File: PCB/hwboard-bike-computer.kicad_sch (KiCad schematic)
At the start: 0 parts

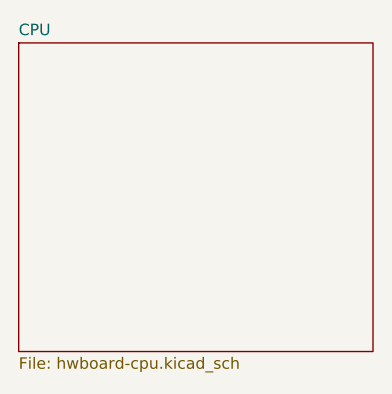
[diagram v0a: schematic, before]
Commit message: Remove temporary and configuration files related to the bike computer project, including lock, PCB, PRL, and project files.
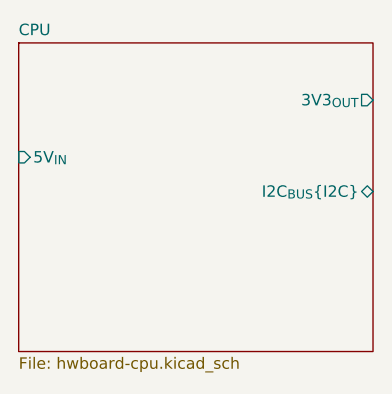
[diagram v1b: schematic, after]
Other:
- sheet CPU ports: added 3V3_{OUT}, 5V_{IN}, I2C_{BUS}{I2C}; removed none
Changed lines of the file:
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@@
+			)
+		)
+		(pin "3V3_{OUT}" output
+			(at 170.18 88.9 0)
+			(effects
+				(font
+					(size 1.27 1.27)
+				)
+				(justify right)
+			)
+		)
+		(pin "I2C_{BUS}{I2C}" bidirectional
+			(at 170.18 99.06 0)
+			(effects
+				(font
+					(size 1.27 1.27)
+				)
+				(justify right)
+			)
+		)
+		(pin "5V_{IN}" input
+			(at 130.81 95.25 180)
+			(effects
+				(font
+					(size 1.27 1.27)
+				)
+				(justify left)
 			)
 		)

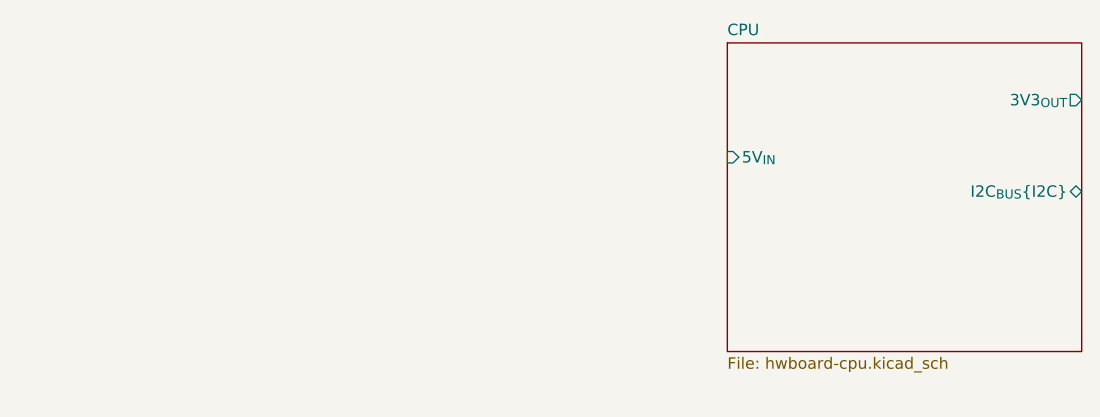
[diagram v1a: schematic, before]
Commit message: add gnss schematics and footprint
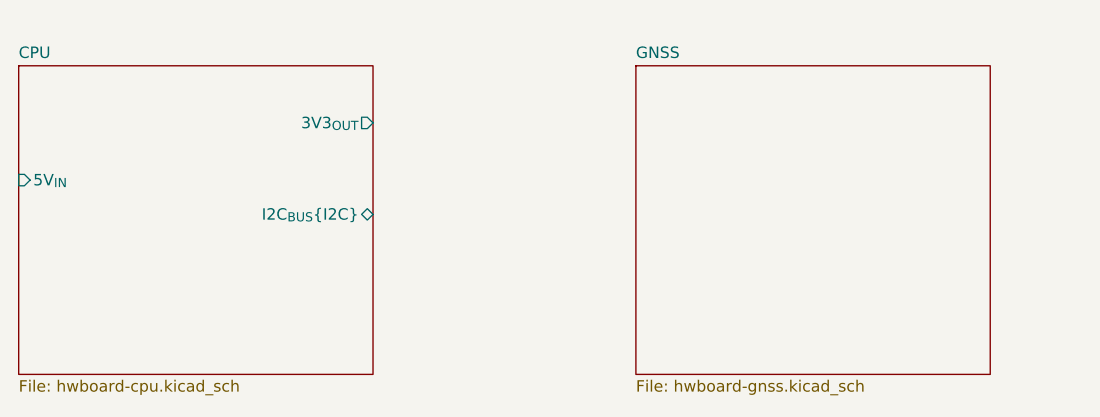
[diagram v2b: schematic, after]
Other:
- added sheet GNSS (hwboard-gnss.kicad_sch)
- title: (none) -> HWBoard Bike Computer
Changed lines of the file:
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@@
 	(generator_version "9.0")
 	(paper "A4")
+	(title_block
+		(title "HWBoard Bike Computer")
+		(date "2025-10-22")
+		(rev "0.1")
+	)
 	(sheet
-		(at 130.81 82.55)
+		(at 52.07 85.09)
 		(size 39.37 34.29)
 		(exclude_from_sim no)
@@
 		)
 		(property "Sheetname" "CPU"
-			(at 130.81 81.8384 0)
+			(at 52.07 84.3784 0)
 			(effects
 				(font
@@
 		)
 		(property "Sheetfile" "hwboard-cpu.kicad_sch"
-			(at 130.81 117.4246 0)
+			(at 52.07 119.9646 0)
 			(effects
 				(font
@@
 		)
 		(pin "3V3_{OUT}" output
-			(at 170.18 88.9 0)
+			(at 91.44 91.44 0)
 			(effects
 				(font
@@
 		)
 		(pin "I2C_{BUS}{I2C}" bidirectional
-			(at 170.18 99.06 0)
+			(at 91.44 101.6 0)
 			(effects
 				(font
@@
 		)
 		(pin "5V_{IN}" input
-			(at 130.81 95.25 180)
+			(at 52.07 97.79 180)
 			(effects
 				(font
@@
 				)
 			)
+		)
+	)
+	(sheet
+		(at 120.65 85.09)
+		(size 39.37 34.29)
+		(exclude_from_sim no)
+		(in_bom yes)
+		(on_board yes)
+		(dnp no)
+		(fields_autoplaced yes)
+		(stroke
+			(width 0.1524)
+			(type solid)
+		)
+		(fill
+			(color 0 0 0 0.0000)
+		)
+		(property "Sheetname" "GNSS"
+			(at 120.65 84.3784 0)
+			(effects
+				(font
+					(size 1.27 1.27)
+				)
+				(justify left bottom)
+			)
+		)
+		(property "Sheetfile" "hwboard-gnss.kicad_sch"
+			(at 120.65 119.9646 0)
+			(effects
+				(font
+					(size 1.27 1.27)
+				)
+				(justify left top)
+			)
+		)
+		(instances
+			(project "hwboard-bike-computer"
+				(path "/8c0f76b9-ee42-4bcf-bb95-09772e367402"
+					(page "3")
+				)
+			)

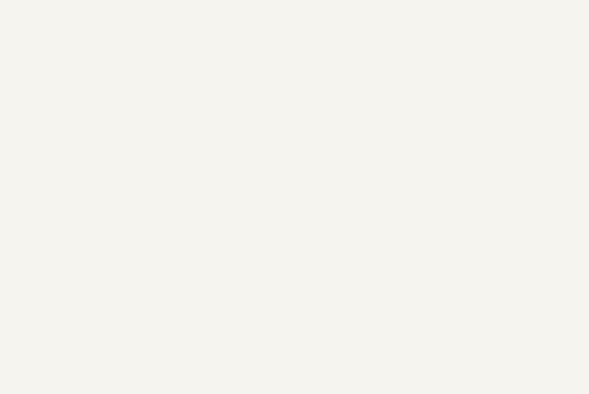
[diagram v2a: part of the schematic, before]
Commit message: add screen sheet
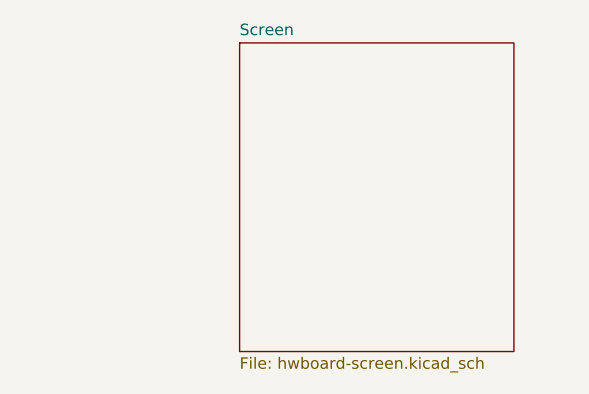
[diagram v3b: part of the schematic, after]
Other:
- added sheet Screen (hwboard-screen.kicad_sch)
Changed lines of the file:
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@@
+	)
+	(sheet
+		(at 201.93 85.09)
+		(size 30.48 34.29)
+		(exclude_from_sim no)
+		(in_bom yes)
+		(on_board yes)
+		(dnp no)
+		(fields_autoplaced yes)
+		(stroke
+			(width 0.1524)
+			(type solid)
+		)
+		(fill
+			(color 0 0 0 0.0000)
+		)
+		(property "Sheetname" "Screen"
+			(at 201.93 84.3784 0)
+			(effects
+				(font
+					(size 1.27 1.27)
+				)
+				(justify left bottom)
+			)
+		)
+		(property "Sheetfile" "hwboard-screen.kicad_sch"
+			(at 201.93 119.9646 0)
+			(effects
+				(font
+					(size 1.27 1.27)
+				)
+				(justify left top)
+			)
+		)
+		(instances
+			(project "hwboard-bike-computer"
+				(path "/8c0f76b9-ee42-4bcf-bb95-09772e367402"
+					(page "4")
+				)
+			)
+		)
 	)
 	(sheet

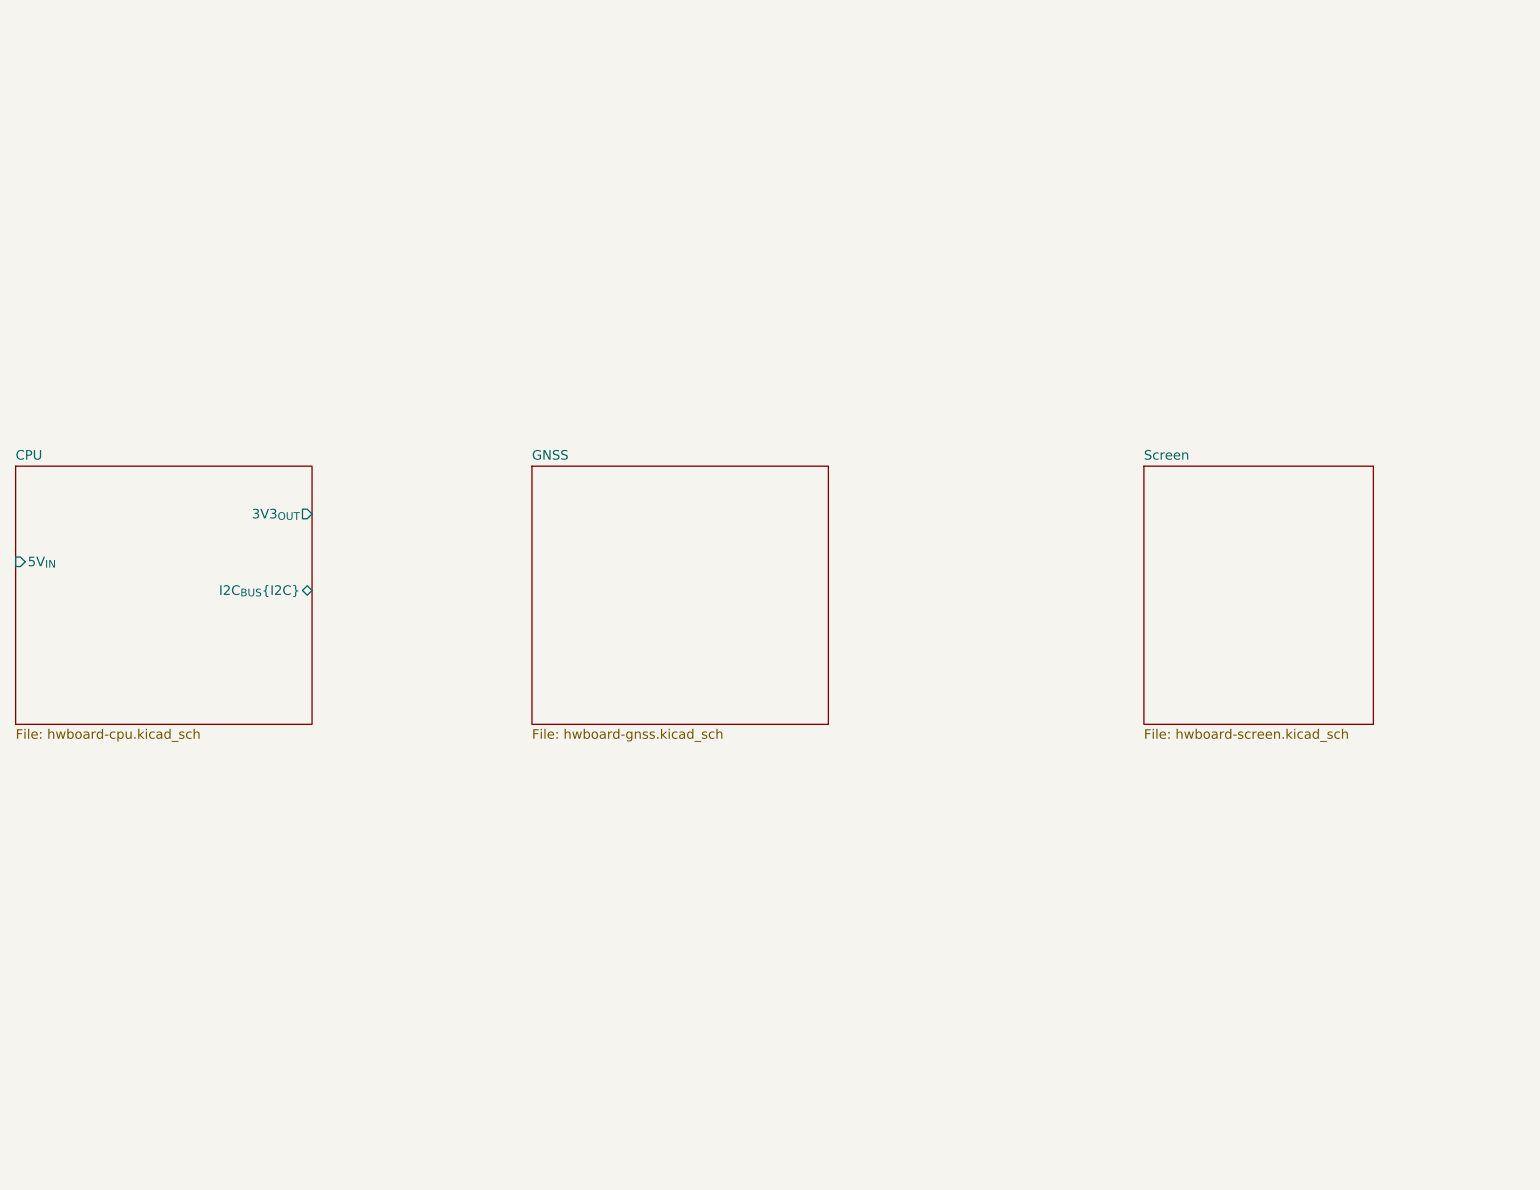
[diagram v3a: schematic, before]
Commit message: add others hierarchicals sheets
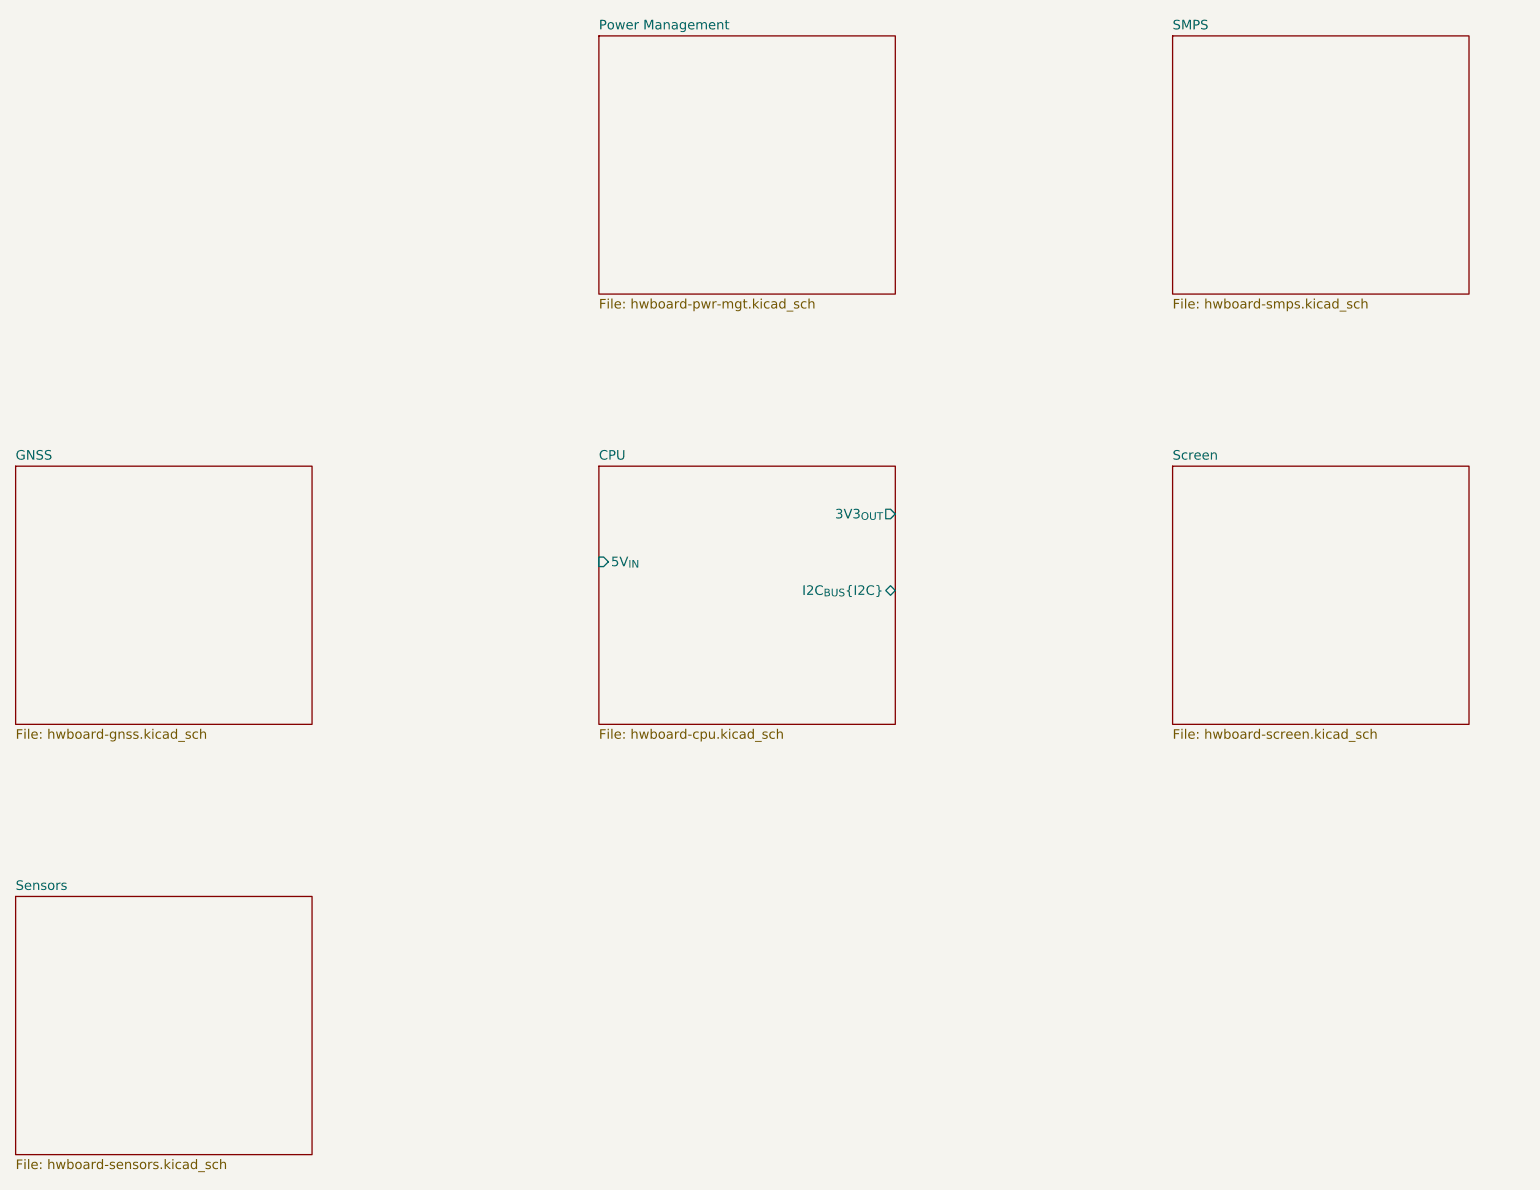
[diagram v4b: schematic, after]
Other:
- added sheet Power Management (hwboard-pwr-mgt.kicad_sch)
- added sheet SMPS (hwboard-smps.kicad_sch)
- added sheet Sensors (hwboard-sensors.kicad_sch)
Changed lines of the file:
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@@
+	)
+	(sheet
+		(at 52.07 142.24)
+		(size 39.37 34.29)
+		(exclude_from_sim no)
+		(in_bom yes)
+		(on_board yes)
+		(dnp no)
+		(fields_autoplaced yes)
+		(stroke
+			(width 0.1524)
+			(type solid)
+		)
+		(fill
+			(color 0 0 0 0.0000)
+		)
+		(property "Sheetname" "Sensors"
+			(at 52.07 141.5284 0)
+			(effects
+				(font
+					(size 1.27 1.27)
+				)
+				(justify left bottom)
+			)
+		)
+		(property "Sheetfile" "hwboard-sensors.kicad_sch"
+			(at 52.07 177.1146 0)
+			(effects
+				(font
+					(size 1.27 1.27)
+				)
+				(justify left top)
+			)
+		)
+		(instances
+			(project "hwboard-bike-computer"
+				(path "/8c0f76b9-ee42-4bcf-bb95-09772e367402"
+					(page "7")
+				)
+			)
+		)
+	)
+	(sheet
+		(at 129.54 85.09)
+		(size 39.37 34.29)
+		(exclude_from_sim no)
+		(in_bom yes)
+		(on_board yes)
+		(dnp no)
+		(fields_autoplaced yes)
+		(stroke
+			(width 0.1524)
+			(type solid)
+		)
+		(fill
+			(color 0 0 0 0.0000)
+		)
+		(property "Sheetname" "CPU"
+			(at 129.54 84.3784 0)
+			(effects
+				(font
+					(size 1.27 1.27)
+				)
+				(justify left bottom)
+			)
+		)
+		(property "Sheetfile" "hwboard-cpu.kicad_sch"
+			(at 129.54 119.9646 0)
+			(effects
+				(font
+					(size 1.27 1.27)
+				)
+				(justify left top)
+			)
+		)
+		(pin "3V3_{OUT}" output
+			(at 168.91 91.44 0)
+			(effects
+				(font
+					(size 1.27 1.27)
+				)
+				(justify right)
+			)
+		)
+		(pin "I2C_{BUS}{I2C}" bidirectional
+			(at 168.91 101.6 0)
+			(effects
+				(font
+					(size 1.27 1.27)
+				)
+				(justify right)
+			)
+		)
+		(pin "5V_{IN}" input
+			(at 129.54 97.79 180)
+			(effects
+				(font
+					(size 1.27 1.27)
+				)
+				(justify left)
+			)
+		)
+		(instances
+			(project "hwboard-bike-computer"
+				(path "/8c0f76b9-ee42-4bcf-bb95-09772e367402"
+					(page "2")
+				)
+			)
+		)
+	)
+	(sheet
+		(at 205.74 85.09)
+		(size 39.37 34.29)
+		(exclude_from_sim no)
+		(in_bom yes)
+		(on_board yes)
+		(dnp no)
+		(fields_autoplaced yes)
+		(stroke
+			(width 0.1524)
+			(type solid)
+		)
+		(fill
+			(color 0 0 0 0.0000)
+		)
+		(property "Sheetname" "Screen"
+			(at 205.74 84.3784 0)
+			(effects
+				(font
+					(size 1.27 1.27)
+				)
+				(justify left bottom)
+			)
+		)
+		(property "Sheetfile" "hwboard-screen.kicad_sch"
+			(at 205.74 119.9646 0)
+			(effects
+				(font
+					(size 1.27 1.27)
+				)
+				(justify left top)
+			)
+		)
+		(instances
+			(project "hwboard-bike-computer"
+				(path "/8c0f76b9-ee42-4bcf-bb95-09772e367402"
+					(page "4")
+				)
+			)
+		)
+	)
+	(sheet
+		(at 129.54 27.94)
+		(size 39.37 34.29)
+		(exclude_from_sim no)
+		(in_bom yes)
+		(on_board yes)
+		(dnp no)
+		(fields_autoplaced yes)
+		(stroke
+			(width 0.1524)
+			(type solid)
+		)
+		(fill
+			(color 0 0 0 0.0000)
+		)
+		(property "Sheetname" "Power Management"
+			(at 129.54 27.2284 0)
+			(effects
+				(font
+					(size 1.27 1.27)
+				)
+				(justify left bottom)
+			)
+		)
+		(property "Sheetfile" "hwboard-pwr-mgt.kicad_sch"
+			(at 129.54 62.8146 0)
+			(effects
+				(font
+					(size 1.27 1.27)
+				)
+				(justify left top)
+			)
+		)
+		(instances
+			(project "hwboard-bike-computer"
+				(path "/8c0f76b9-ee42-4bcf-bb95-09772e367402"
+					(page "5")
+				)
+			)
+		)
+	)
+	(sheet
+		(at 205.74 27.94)
+		(size 39.37 34.29)
+		(exclude_from_sim no)
+		(in_bom yes)
+		(on_board yes)
+		(dnp no)
+		(fields_autoplaced yes)
+		(stroke
+			(width 0.1524)
+			(type solid)
+		)
+		(fill
+			(color 0 0 0 0.0000)
+		)
+		(property "Sheetname" "SMPS"
+			(at 205.74 27.2284 0)
+			(effects
+				(font
+					(size 1.27 1.27)
+				)
+				(justify left bottom)
+			)
+		)
+		(property "Sheetfile" "hwboard-smps.kicad_sch"
+			(at 205.74 62.8146 0)
+			(effects
+				(font
+					(size 1.27 1.27)
+				)
+				(justify left top)
+			)
+		)
+		(instances
+			(project "hwboard-bike-computer"
+				(path "/8c0f76b9-ee42-4bcf-bb95-09772e367402"
+					(page "6")
+				)
+			)
+		)
 	)
 	(sheet
@@
 			(color 0 0 0 0.0000)
 		)
-		(property "Sheetname" "CPU"
+		(property "Sheetname" "GNSS"
 			(at 52.07 84.3784 0)
 			(effects
@@
 			)
 		)
-		(property "Sheetfile" "hwboard-cpu.kicad_sch"
+		(property "Sheetfile" "hwboard-gnss.kicad_sch"
 			(at 52.07 119.9646 0)
 			(effects
 				(font
-					(size 1.27 1.27)
-				)
-				(justify left top)
-			)
-		)
-		(pin "3V3_{OUT}" output
-			(at 91.44 91.44 0)
-			(effects
-				(font
-					(size 1.27 1.27)
-				)
-				(justify right)
-			)
-		)
-		(pin "I2C_{BUS}{I2C}" bidirectional
-			(at 91.44 101.6 0)
-			(effects
-				(font
-					(size 1.27 1.27)
-				)
-				(justify right)
-			)
-		)
-		(pin "5V_{IN}" input
-			(at 52.07 97.79 180)
-			(effects
-				(font
-					(size 1.27 1.27)
-				)
-				(justify left)
-			)
-		)
-		(instances
-			(project "hwboard-bike-computer"
-				(path "/8c0f76b9-ee42-4bcf-bb95-09772e367402"
-					(page "2")
-				)
-			)
-		)
-	)
-	(sheet
-		(at 201.93 85.09)
-		(size 30.48 34.29)
-		(exclude_from_sim no)
-		(in_bom yes)
-		(on_board yes)
-		(dnp no)
-		(fields_autoplaced yes)
-		(stroke
-			(width 0.1524)
-			(type solid)
-		)
-		(fill
-			(color 0 0 0 0.0000)
-		)
-		(property "Sheetname" "Screen"
-			(at 201.93 84.3784 0)
-			(effects
-				(font
-					(size 1.27 1.27)
-				)
-				(justify left bottom)
-			)
-		)
-		(property "Sheetfile" "hwboard-screen.kicad_sch"
-			(at 201.93 119.9646 0)
-			(effects
-				(font
-					(size 1.27 1.27)
-				)
-				(justify left top)
-			)
-		)
-		(instances
-			(project "hwboard-bike-computer"
-				(path "/8c0f76b9-ee42-4bcf-bb95-09772e367402"
-					(page "4")
-				)
-			)
-		)
-	)
-	(sheet
-		(at 120.65 85.09)
-		(size 39.37 34.29)
-		(exclude_from_sim no)
-		(in_bom yes)
-		(on_board yes)
-		(dnp no)
-		(fields_autoplaced yes)
-		(stroke
-			(width 0.1524)
-			(type solid)
-		)
-		(fill
-			(color 0 0 0 0.0000)
-		)
-		(property "Sheetname" "GNSS"
-			(at 120.65 84.3784 0)
-			(effects
-				(font
-					(size 1.27 1.27)
-				)
-				(justify left bottom)
-			)
-		)
-		(property "Sheetfile" "hwboard-gnss.kicad_sch"
-			(at 120.65 119.9646 0)
-			(effects
-				(font
